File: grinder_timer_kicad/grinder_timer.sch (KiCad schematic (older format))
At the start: 21 parts, among them IC1 ATMEGA328P-P, T1 TRANS, U1 SSD1306_128x64OLED, U2 serial_to_usb, U3 LM7805CT

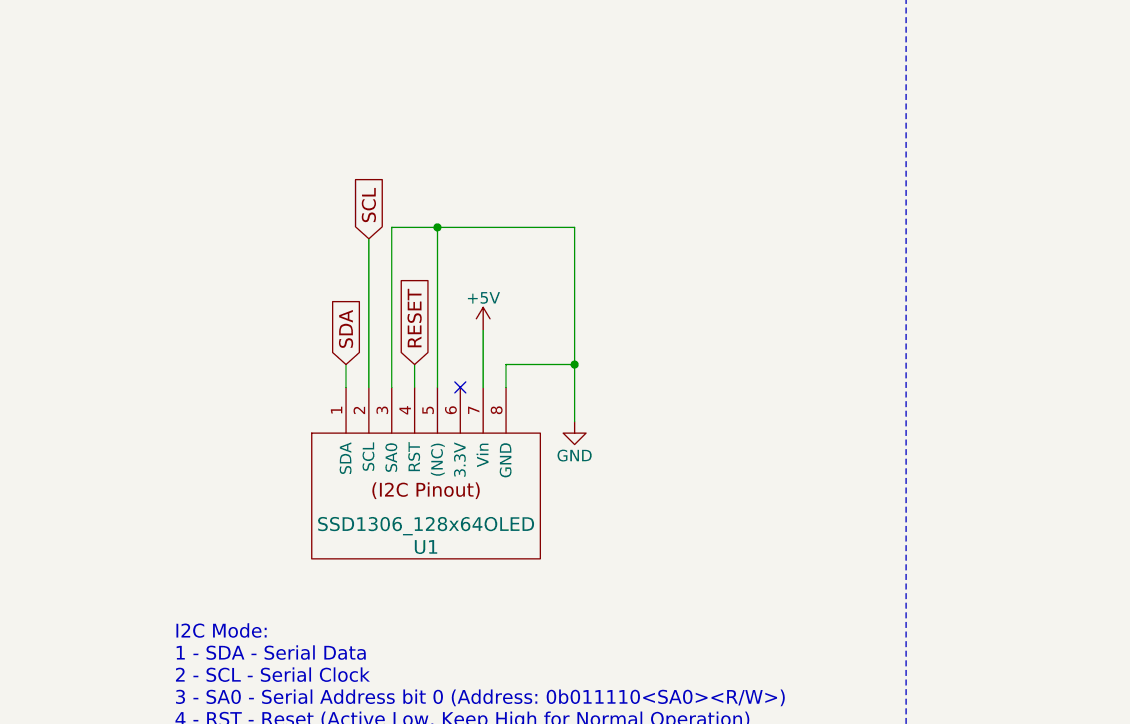
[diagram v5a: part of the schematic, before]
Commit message: Added a capacitor across oled rest pin to simulate reset toggle on power-up.
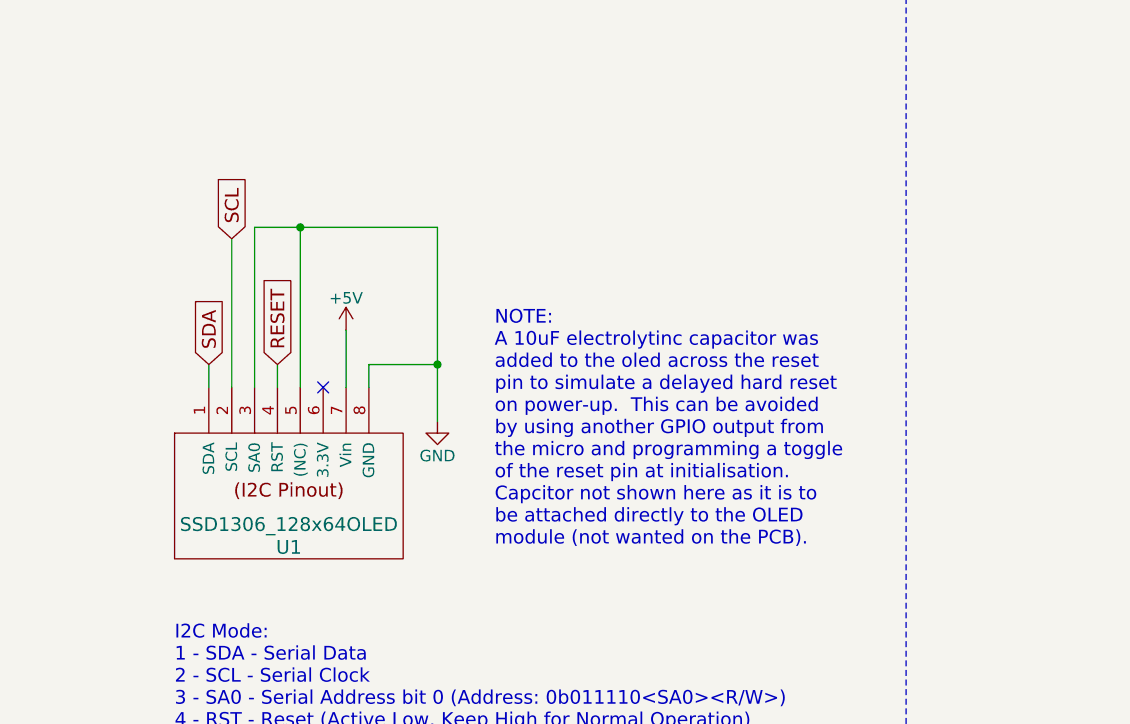
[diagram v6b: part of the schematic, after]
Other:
- note added: "NOTE:\nA 10uF electrolytinc capacitor was\nadded to the oled across the reset\npin to simulate a delayed hard reset\non power-up. This can be avoided\nby using another GPIO output from\nthe micro and programming a toggle\nof the reset pin at initialisation.\nCapcitor not shown here as it is to\nbe attached directly to the OLED\nmodule (not wanted on the PCB)."
- moved on the sheet: U1
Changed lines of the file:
@@
 L SSD1306_128x64OLED U1
 U 1 1 5A08DA65
-P 9050 3800
-F 0 "U1" H 9050 3300 60  0000 C CNN
-F 1 "SSD1306_128x64OLED" H 9050 3400 60  0000 C CNN
-F 2 "Pin_Headers:Pin_Header_Straight_1x08" H 9050 4250 60  0001 C CNN
-F 3 "" H 9050 4250 60  0001 C CNN
-	1    9050 3800
-	1    0    0    -1
-$EndComp
-Text GLabel 8700 3500 1    60   Input ~ 0
+P 8450 3800
+F 0 "U1" H 8450 3300 60  0000 C CNN
+F 1 "SSD1306_128x64OLED" H 8450 3400 60  0000 C CNN
+F 2 "Pin_Headers:Pin_Header_Straight_1x08" H 8450 4250 60  0001 C CNN
+F 3 "" H 8450 4250 60  0001 C CNN
+	1    8450 3800
+	1    0    0    -1
+$EndComp
+Text GLabel 8100 3500 1    60   Input ~ 0
 SDA
-Text GLabel 8800 2950 1    60   Input ~ 0
+Text GLabel 8200 2950 1    60   Input ~ 0
 SCL
 Text GLabel 4400 4750 2    60   Input ~ 0
@@
 Text GLabel 3450 3800 2    60   Input ~ 0
 MISO
-Text GLabel 9000 3500 1    60   Input ~ 0
+Text GLabel 8400 3500 1    60   Input ~ 0
 RESET
 $Comp
@@
 NoConn ~ 3000 3500
 NoConn ~ 3000 3400
-NoConn ~ 9200 3600
+NoConn ~ 8600 3600
 $Comp
 L D_Bridge_+-AA D_RECT1
@@
 	7750 1250 7450 1250
 Wire Wire Line
-	9400 3600 9400 3500
-Wire Wire Line
-	9400 3500 9700 3500
-Wire Wire Line
-	9700 2900 9700 3750
-Wire Wire Line
-	9100 2900 9100 3600
-Connection ~ 9700 3500
-Wire Wire Line
-	8900 2900 8900 3600
-Wire Wire Line
-	9000 3600 9000 3500
-Wire Wire Line
-	8700 3600 8700 3500
-Wire Wire Line
-	8800 2950 8800 3600
+	8800 3600 8800 3500
+Wire Wire Line
+	8800 3500 9100 3500
+Wire Wire Line
+	9100 2900 9100 3750
+Wire Wire Line
+	8500 2900 8500 3600
+Connection ~ 9100 3500
+Wire Wire Line
+	8300 2900 8300 3600
+Wire Wire Line
+	8400 3600 8400 3500
+Wire Wire Line
+	8100 3600 8100 3500
+Wire Wire Line
+	8200 2950 8200 3600
 Wire Wire Line
 	7450 1250 7450 1200
@@
 	3000 5400 3650 5400
 Wire Wire Line
-	9300 3350 9300 3600
+	8700 3350 8700 3600
 Wire Wire Line
 	8000 1450 8350 1450
@@
 Connection ~ 850  3400
 Wire Wire Line
-	8900 2900 9700 2900
-Connection ~ 9100 2900
+	8300 2900 9100 2900
+Connection ~ 8500 2900
 Wire Wire Line
 	4900 4100 4900 4250
@@
 L +5V #PWR019
 U 1 1 5A1ABE2B
-P 9300 3350
-F 0 "#PWR019" H 9300 3200 50  0001 C CNN
-F 1 "+5V" H 9300 3490 50  0000 C CNN
-F 2 "" H 9300 3350 50  0000 C CNN
-F 3 "" H 9300 3350 50  0000 C CNN
-	1    9300 3350
+P 8700 3350
+F 0 "#PWR019" H 8700 3200 50  0001 C CNN
+F 1 "+5V" H 8700 3490 50  0000 C CNN
+F 2 "" H 8700 3350 50  0000 C CNN
+F 3 "" H 8700 3350 50  0000 C CNN
+	1    8700 3350
 	1    0    0    -1
 $EndComp
@@
 L GND #PWR020
 U 1 1 5A1ABE75
-P 9700 3750
-F 0 "#PWR020" H 9700 3500 50  0001 C CNN
-F 1 "GND" H 9700 3600 50  0000 C CNN
-F 2 "" H 9700 3750 50  0000 C CNN
-F 3 "" H 9700 3750 50  0000 C CNN
-	1    9700 3750
-	1    0    0    -1
-$EndComp
+P 9100 3750
+F 0 "#PWR020" H 9100 3500 50  0001 C CNN
+F 1 "GND" H 9100 3600 50  0000 C CNN
+F 2 "" H 9100 3750 50  0000 C CNN
+F 3 "" H 9100 3750 50  0000 C CNN
+	1    9100 3750
+	1    0    0    -1
+$EndComp
+Text Notes 9350 4300 0    60   ~ 0
+NOTE:\nA 10uF electrolytinc capacitor was\nadded to the oled across the reset\npin to simulate a delayed hard reset\non power-up.  This can be avoided\nby using another GPIO output from\nthe micro and programming a toggle\nof the reset pin at initialisation.\nCapcitor not shown here as it is to\nbe attached directly to the OLED\nmodule (not wanted on the PCB).
 $EndSCHEMATC

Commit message: Tidied schematic and pcb border.
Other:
- note added: "04/12/2017"
- note added: "1"
- note added: "OLED Module with SSD1306 Driver"
- note added: "grinder_timer"
- note added: "refer to https://github.com/Clewsy/grinder_timer"
- moved on the sheet: Active1, Button_Header1, C1, C2, C3, C4, D_RECT1, IC1, Motor1, Neutral1, RELAY1, RESET1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

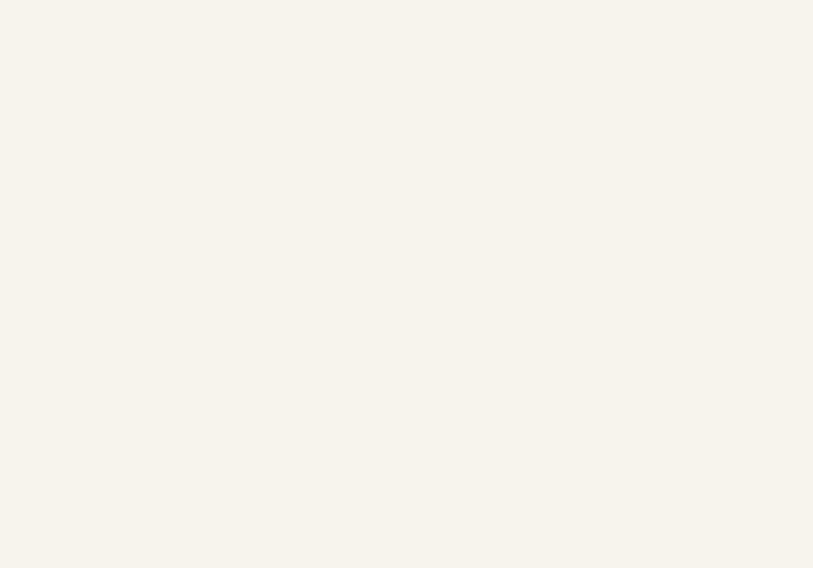
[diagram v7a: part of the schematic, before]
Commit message: Added a reference schematic of the rancilio rocky coffee grinder.
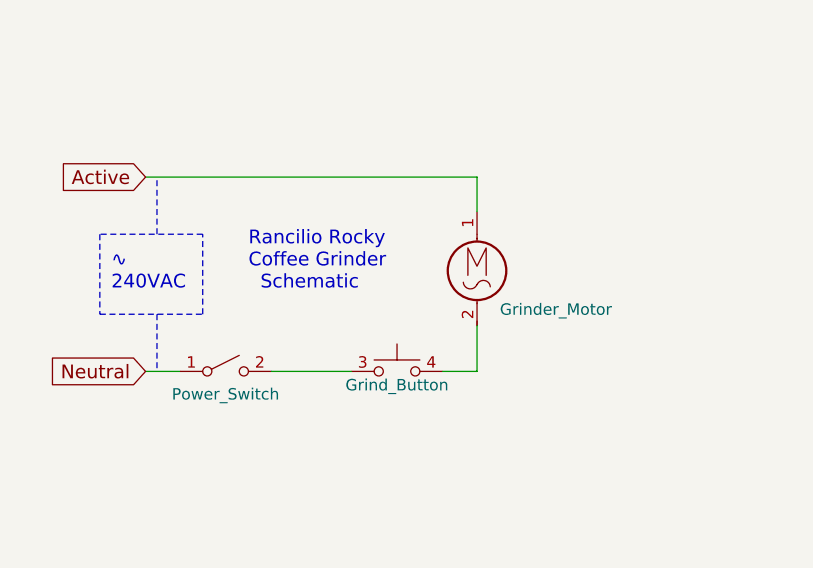
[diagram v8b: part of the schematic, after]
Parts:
- added M?: Grinder_Motor, symbol Motor_AC
- added SW?: Grind_Button, symbol SW_Push_Dual_x2
- added SW?: Power_Switch, symbol SW_DPST_x2
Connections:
- new net: M?.2, SW?.4 (B)
- new net: SW?.2 (B), SW?.3 (A)
- new net Active: M?.1
- new net Neutral: SW?.1 (A)
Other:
- note added: "Rancilio Rocky\nCoffee Grinder\n Schematic"
- note added: "∿\n240VAC"
